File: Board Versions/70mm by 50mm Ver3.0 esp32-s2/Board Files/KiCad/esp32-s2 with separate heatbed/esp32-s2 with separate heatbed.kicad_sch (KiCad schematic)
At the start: 21 parts

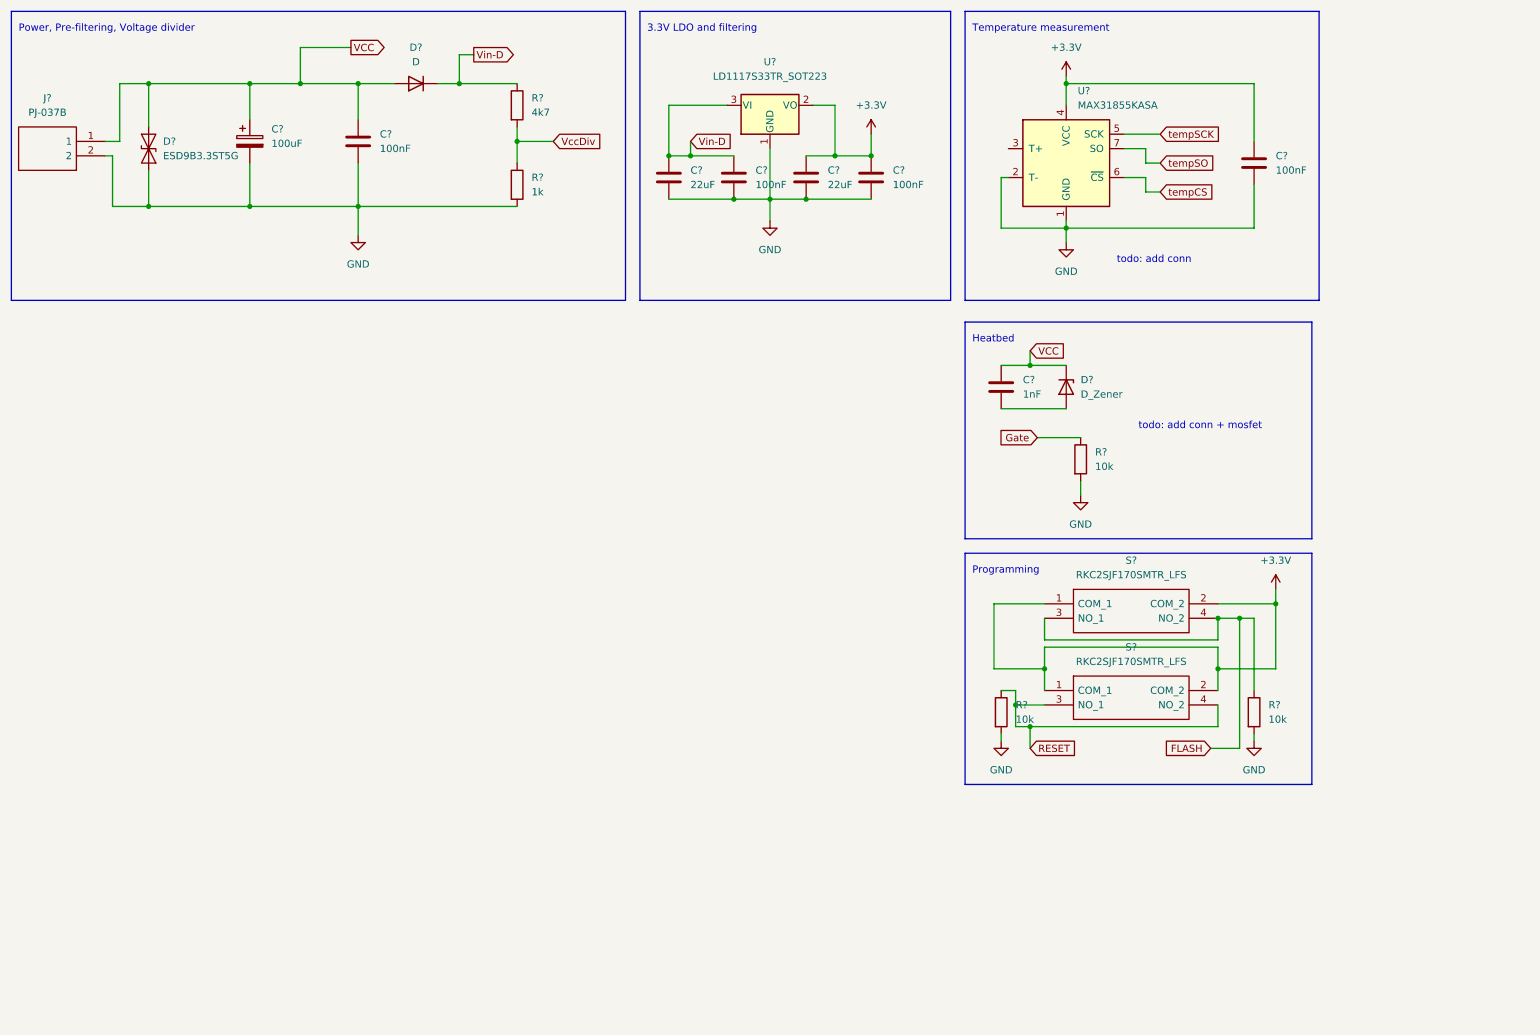
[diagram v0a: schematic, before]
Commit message: Add esp32-s2, not routed
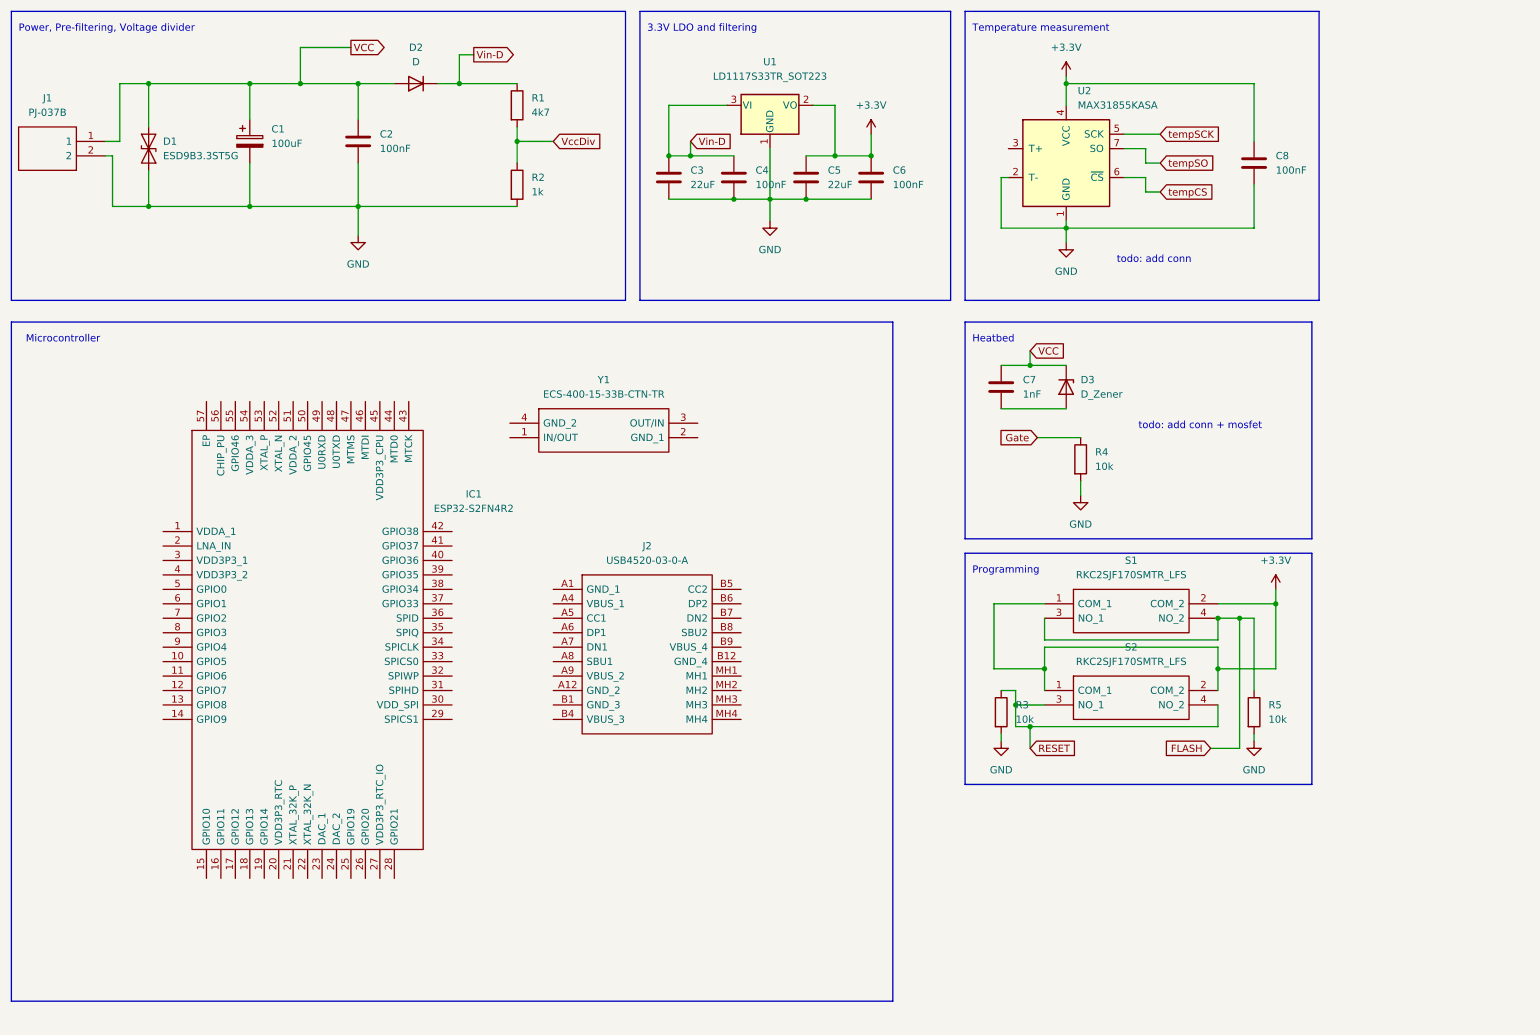
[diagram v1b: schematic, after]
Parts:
- added IC1: ESP32-S2FN4R2, QFN40P700X700X90-57N-D, symbol library_loader:ESP32-S2FN4R2
- added J2: USB4520-03-0-A, USB4520030A, symbol library_loader:USB4520-03-0-A
- added Y1: ECS-400-15-33B-CTN-TR, ECS2501033BCKMTR, symbol library_loader:ECS-400-15-33B-CTN-TR
- gave numbers to parts that had none: 21
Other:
- note added: "Microcontroller"

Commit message: Microcontrolling schematics, not complete
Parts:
- added C? (x6): 100nF, symbol Device:C
- added C?: 10uF, symbol Device:C
- added C? (x2): 15pF, symbol Device:C
- added C?: 100pF, symbol Device:C
- added C? (x3): 1uF, symbol Device:C
- added R? (x2): 5k1, symbol Device:R
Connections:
- net +3V3: now also IC1.1 (VDDA_1), IC1.20 (VDD3P3_RTC), IC1.27 (VDD3P3_RTC_IO), IC1.3 (VDD3P3_1), IC1.30 (VDD_SPI), IC1.4 (VDD3P3_2), IC1.45 (VDD3P3_CPU), IC1.51 (VDDA_2), IC1.54 (VDDA_3), R3.1, R5.1, C?.1, C?.1, C?.1, C?.1, C?.1, C?.1, C?.1, C?.1, C?.1, C?.1, C?.1; no longer S1.1 (COM_1), S1.2 (COM_2), S2.1 (COM_1), S2.2 (COM_2)
- net FLASH: now also R5.2, S2.3 (NO_1), S2.4 (NO_2); no longer R5.1, S1.3 (NO_1), S1.4 (NO_2)
- net GND: now also IC1.57 (EP), J2.A1 (GND_1), J2.A12 (GND_2), J2.B1 (GND_3), J2.B12 (GND_4), S1.1 (COM_1), S1.2 (COM_2), S2.1 (COM_1), S2.2 (COM_2), Y1.2 (GND_1), Y1.4 (GND_2), C?.1, C?.2, C?.2, C?.2, C?.2, C?.2, C?.2, C?.2, C?.2, C?.2, C?.2, C?.2, C?.2, R?.1, R?.1; no longer R3.2, R5.2
- net XTAL_P: now reaches Y1.1 (IN/OUT)
- net XTAL_P: now also IC1.53 (XTAL_P), C?.2
- net XTAL_N: now reaches Y1.3 (OUT/IN)
- net XTAL_N: now also IC1.52 (XTAL_N), C?.1
- net VBUS: now reaches J2.A4 (VBUS_1)
- net VBUS: now also J2.A9 (VBUS_2), J2.B4 (VBUS_3), J2.B9 (VBUS_4)
- net at J2.A5 (CC1): now also R?.2
- net D+: now reaches J2.A6 (DP1)
- net D+: now also IC1.26 (GPIO20), J2.B6 (DP2)
- net D-: now reaches J2.A7 (DN1)
- net D-: now also IC1.25 (GPIO19), J2.B7 (DN2)
- net at J2.B5 (CC2): now also R?.2
- net EN: now reaches IC1.56 (CHIP_PU)
- net EN: now also R3.2, S1.3 (NO_1), S1.4 (NO_2)
- removed net RESET: R3.1, S2.3 (NO_1), S2.4 (NO_2)
- no-connect marks 0 -> 14
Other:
- note added: "todo: All VBUS:es or only 1+4?"
- note added: "todo: VDD_SPI?"
- note added: "todo: add back diode"
- note added: "todo: add capacitor for EN?"
- note added: "todo: xtal p+n correctly placed to in/out?"
- moved on the sheet: IC1, J2, R3, R5, S1, S2, Y1

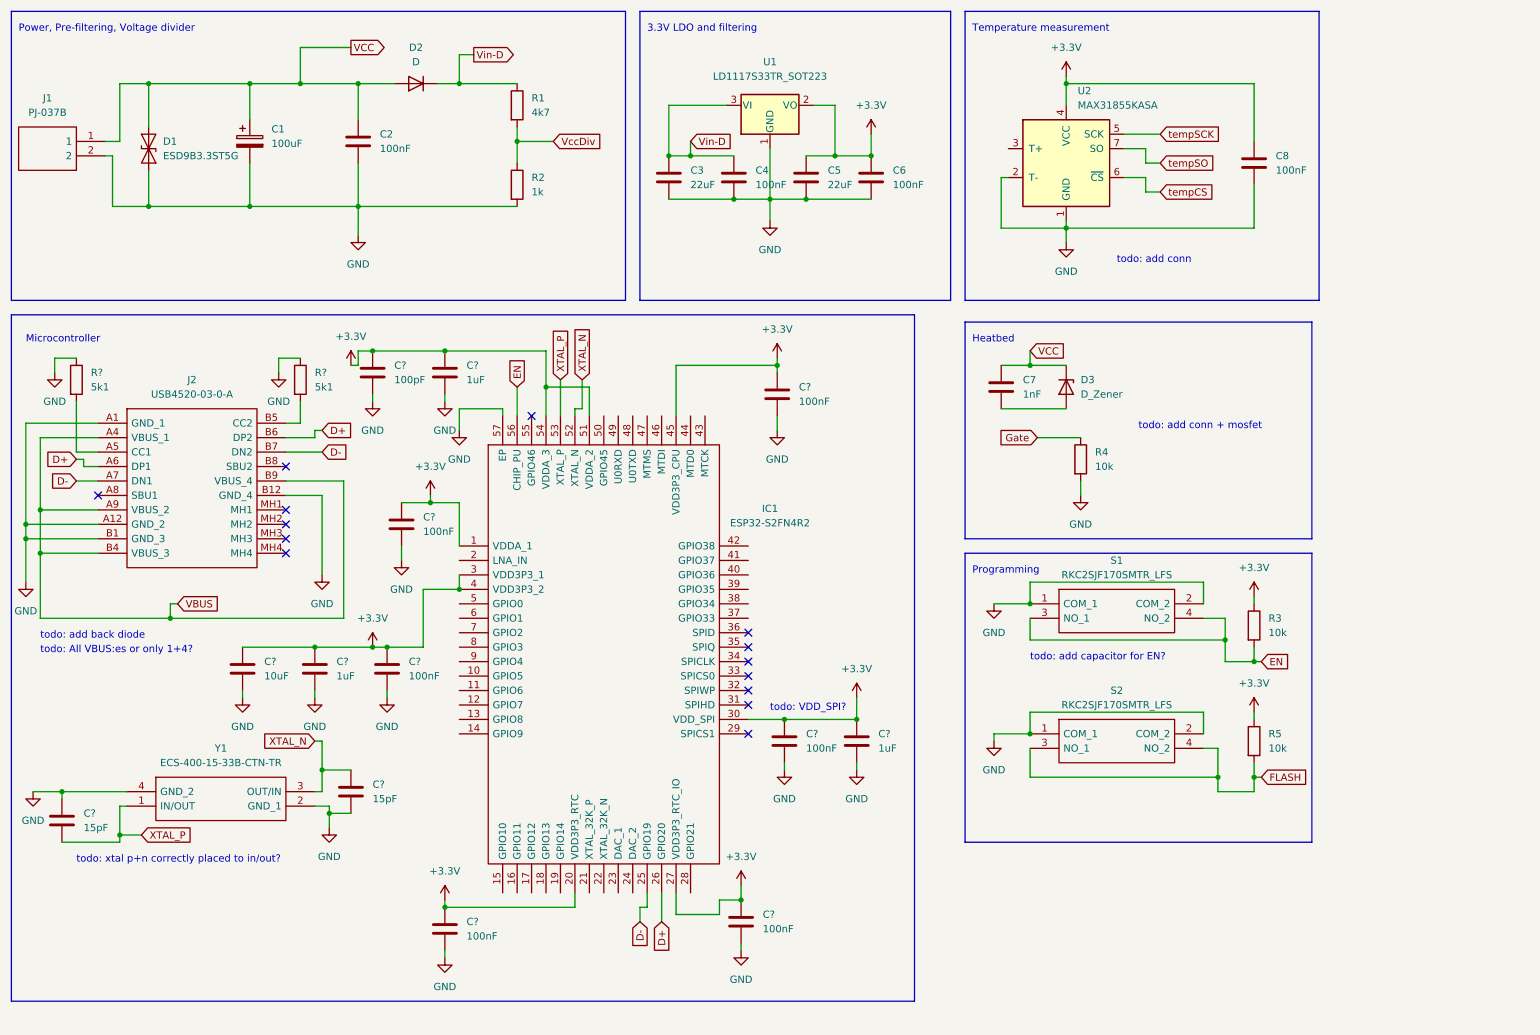
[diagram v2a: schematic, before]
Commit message: Add Antenna + mosfet + connectors
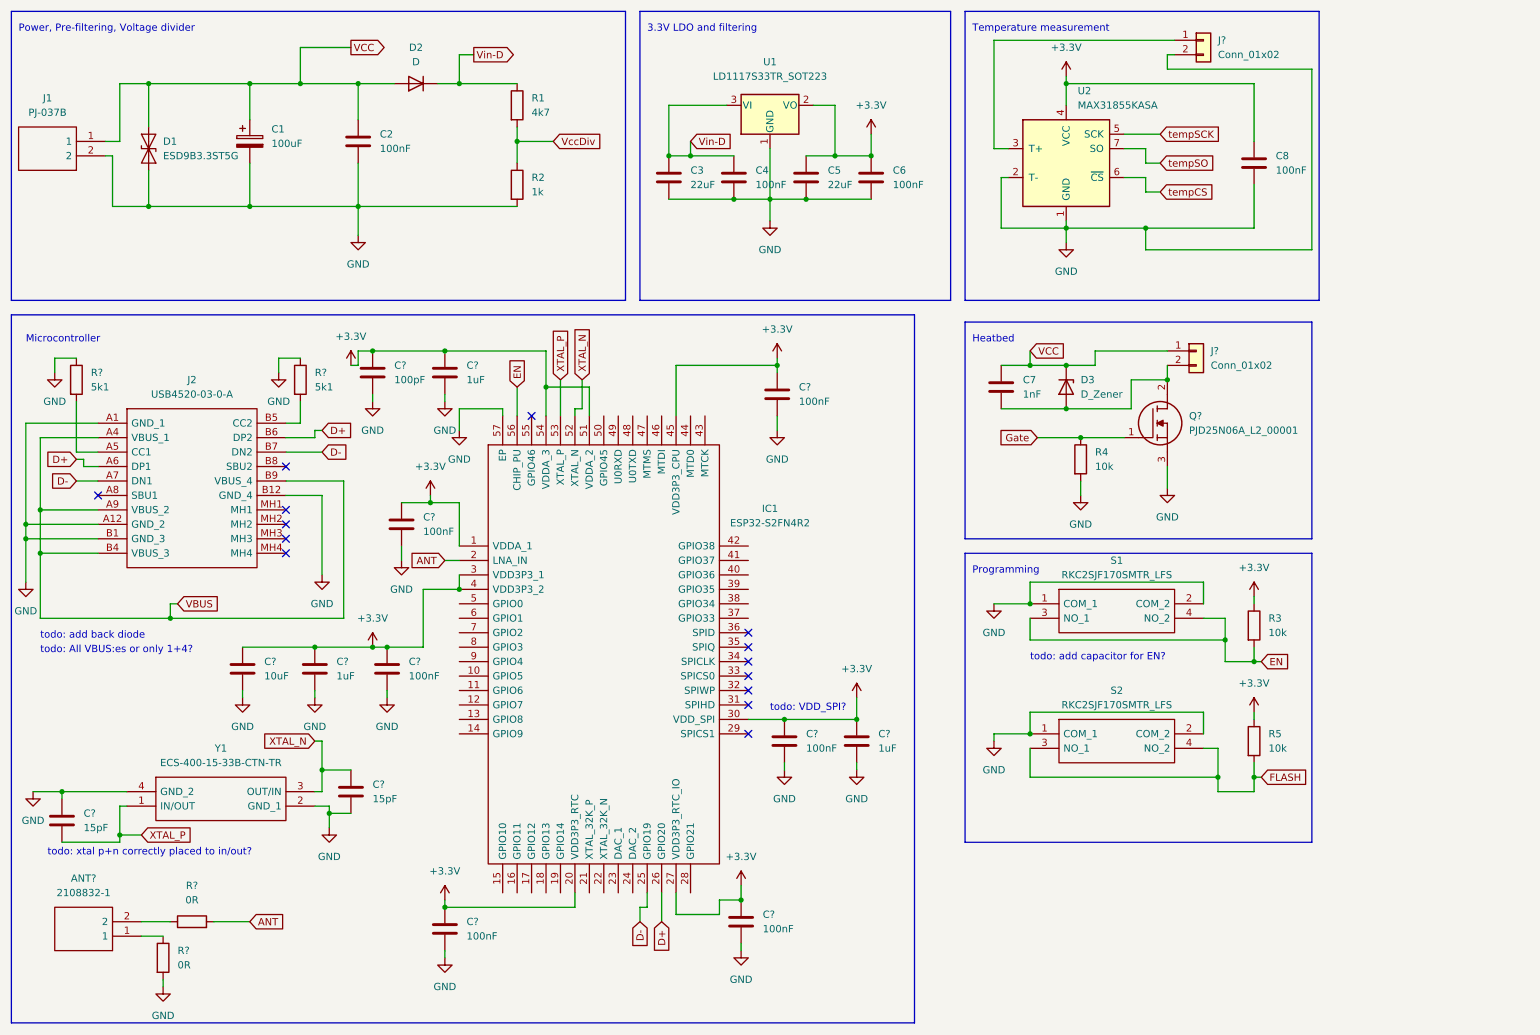
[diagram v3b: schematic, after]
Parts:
- added ANT?: 2108832-1, 21088321, symbol library_loader:2108832-1
- added J? (x2): Conn_01x02, symbol Connector_Generic:Conn_01x02
- added Q?: PJD25N06A_L2_00001, PJD25N06A_L2_00001, symbol library_loader:PJD25N06A_L2_00001
- added R? (x2): 0R, symbol Device:R
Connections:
- net GND: now also J?.2 (Pin_2), Q?.3, R?.2
- net Gate: now also Q?.1
- net VCC: now also J?.1 (Pin_1)
- net at C7.2, D3.2 (A): now also J?.2 (Pin_2), Q?.2
- net ANT: now reaches IC1.2 (LNA_IN)
- net ANT: now also R?.2
- net at U2.3 (T+): now also J?.1 (Pin_1)
- new net: ANT?.1, R?.1
- new net: ANT?.2, R?.1
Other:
- note removed: "todo: add conn"
- note removed: "todo: add conn + mosfet"

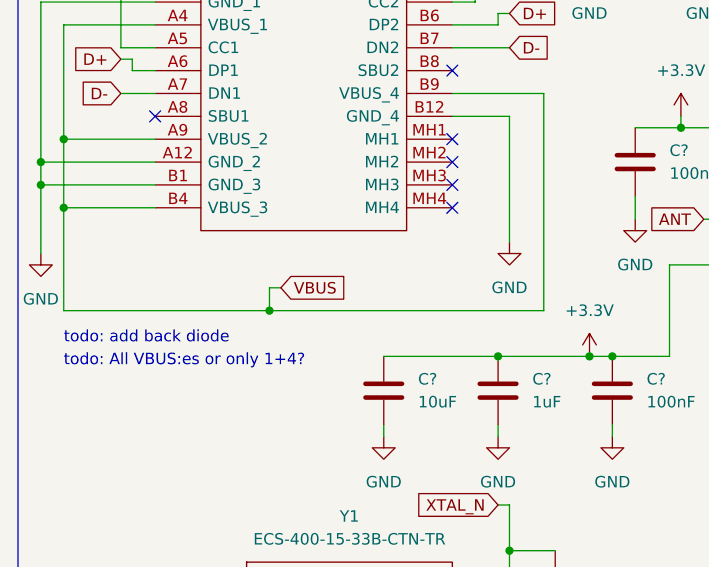
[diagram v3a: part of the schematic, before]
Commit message: Back diode for USB vbus
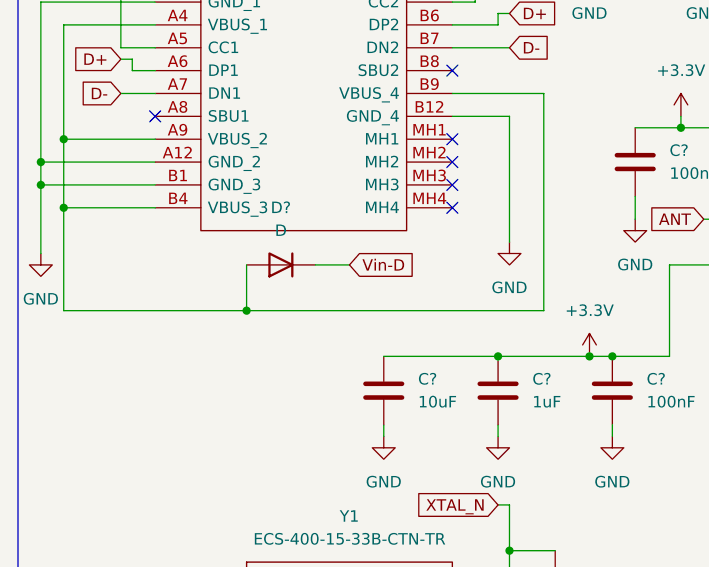
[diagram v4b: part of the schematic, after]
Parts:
- added D?: D, symbol Device:D
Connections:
- net Vin-D: now also D?.1 (K)
- net VBUS: no longer names the net of J2.A4 (VBUS_1), J2.A9 (VBUS_2), J2.B4 (VBUS_3), J2.B9 (VBUS_4)
- net VBUS: now also D?.2 (A)
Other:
- note removed: "todo: All VBUS:es or only 1+4?"
- note removed: "todo: add back diode"
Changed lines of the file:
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@@
   (junction (at 71.12 148.59) (diameter 0) (color 0 0 0 0)
   )
-  (junction (at 44.45 121.92) (diameter 0) (color 0 0 0 0)
-  )
   (junction (at 40.64 49.53) (diameter 0) (color 0 0 0 0)
   )
@@
   )
   (junction (at 228.6 149.86) (diameter 0) (color 0 0 0 0)
+  )
+  (junction (at 41.91 121.92) (diameter 0) (color 0 0 0 0)
   )
   (junction (at 152.4 139.7) (diameter 0) (color 0 0 0 0)
@@
     (stroke (width 0) (type default) (color 0 0 0 0))
   )
+  (wire (pts (xy 41.91 116.84) (xy 41.91 121.92))
+    (stroke (width 0) (type default) (color 0 0 0 0))
+  )
   (wire (pts (xy 195.58 144.78) (xy 195.58 149.86))
     (stroke (width 0) (type default) (color 0 0 0 0))
@@
     (stroke (width 0) (type default) (color 0 0 0 0))
   )
+  (wire (pts (xy 49.53 116.84) (xy 53.34 116.84))
+    (stroke (width 0) (type default) (color 0 0 0 0))
+  )
   (wire (pts (xy 189.23 119.38) (xy 195.58 119.38))
     (stroke (width 0) (type default) (color 0 0 0 0))
@@
     (stroke (width 0) (type default) (color 0 0 0 0))
   )
-  (wire (pts (xy 44.45 119.38) (xy 44.45 121.92))
-    (stroke (width 0) (type default) (color 0 0 0 0))
-  )
   (wire (pts (xy 95.25 116.84) (xy 88.9 116.84))
     (stroke (width 0) (type default) (color 0 0 0 0))
@@
     (stroke (width 0) (type default) (color 0 0 0 0))
   )
-  (wire (pts (xy 45.72 119.38) (xy 44.45 119.38))
-    (stroke (width 0) (type default) (color 0 0 0 0))
-  )
   (wire (pts (xy 95.25 27.94) (xy 105.41 27.94))
     (stroke (width 0) (type default) (color 0 0 0 0))
@@
     (stroke (width 0) (type default) (color 0 0 0 0))
   )
-  (wire (pts (xy 44.45 121.92) (xy 74.93 121.92))
+  (wire (pts (xy 21.59 121.92) (xy 41.91 121.92))
     (stroke (width 0) (type default) (color 0 0 0 0))
   )
@@
     (stroke (width 0) (type default) (color 0 0 0 0))
   )
-  (wire (pts (xy 21.59 121.92) (xy 44.45 121.92))
-    (stroke (width 0) (type default) (color 0 0 0 0))
-  )
   (wire (pts (xy 234.95 129.54) (xy 229.87 129.54))
     (stroke (width 0) (type default) (color 0 0 0 0))
@@
     (stroke (width 0) (type default) (color 0 0 0 0))
   )
+  (wire (pts (xy 41.91 121.92) (xy 74.93 121.92))
+    (stroke (width 0) (type default) (color 0 0 0 0))
+  )
   (wire (pts (xy 213.36 80.01) (xy 213.36 85.09))
     (stroke (width 0) (type default) (color 0 0 0 0))
@@
   (polyline (pts (xy 184.15 110.49) (xy 245.11 110.49))
     (stroke (width 0) (type default) (color 0 0 0 0))
-  )
-  (text "todo: All VBUS:es or only 1+4?" (at 21.59 128.27 0)
-    (effects (font (size 1.27 1.27)) (justify left bottom))
   )
   (text "Heatbed" (at 185.42 73.66 0)
@@
   )
   (text "todo: VDD_SPI?" (at 149.86 138.43 0)
-    (effects (font (size 1.27 1.27)) (justify left bottom))
-  )
-  (text "todo: add back diode" (at 21.59 125.73 0)
     (effects (font (size 1.27 1.27)) (justify left bottom))
   )
@@
     )
   )
-  (global_label "VBUS" (shape input) (at 45.72 119.38 0) (fields_autoplaced)
+  (global_label "Vin-D" (shape input) (at 53.34 116.84 0) (fields_autoplaced)
     (effects (font (size 1.27 1.27)) (justify left))
-    (property "Intersheet References" "${INTERSHEET_REFS}" (id 0) (at 53.0317 119.3006 0)
+    (property "Intersheet References" "${INTERSHEET_REFS}" (id 0) (at 61.4379 116.7606 0)
       (effects (font (size 1.27 1.27)) (justify left) hide)
     )
@@
     )
     (pin "1")
+  )
+  (symbol (lib_id "Device:D") (at 45.72 116.84 180) (unit 1)
+    (in_bom yes) (on_board yes) (fields_autoplaced)
+    (property "Reference" "D?" (id 0) (at 45.72 110.49 0))
+    (property "Value" "D" (id 1) (at 45.72 113.03 0))
+    (property "Footprint" "" (id 2) (at 45.72 116.84 0)
+      (effects (font (size 1.27 1.27)) hide)
+    )
+    (property "Datasheet" "~" (id 3) (at 45.72 116.84 0)
+      (effects (font (size 1.27 1.27)) hide)
+    )
+    (pin "1")
+    (pin "2")
   )
   (symbol (lib_id "power:GND") (at 19.05 115.57 0) (unit 1)
@@
       (reference "D3") (unit 1) (value "D_Zener") (footprint "")
     )
+    (path "/7c9c17f7-2c1d-4e33-a4f0-562d9266a71f"
+      (reference "D?") (unit 1) (value "D") (footprint "")
+    )
     (path "/c09c1b92-ad43-4b68-8a16-c538c052dabe"
